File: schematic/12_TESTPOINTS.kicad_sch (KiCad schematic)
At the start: 10 parts

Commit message: Exclude JP1, JP2, TP1-TP20 from BOM (attrs only, sch+pcb)
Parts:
- TP11, TP12, TP13, TP14, TP15, TP16, TP17, TP18, TP19, TP20: now left out of the parts list
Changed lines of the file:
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@@
 		(unit 1)
 		(exclude_from_sim no)
-		(in_bom yes)
+		(in_bom no)
 		(on_board yes)
 		(dnp no)
@@
 		(unit 1)
 		(exclude_from_sim no)
-		(in_bom yes)
+		(in_bom no)
 		(on_board yes)
 		(dnp no)
@@
 		(unit 1)
 		(exclude_from_sim no)
-		(in_bom yes)
+		(in_bom no)
 		(on_board yes)
 		(dnp no)
@@
 		(unit 1)
 		(exclude_from_sim no)
-		(in_bom yes)
+		(in_bom no)
 		(on_board yes)
 		(dnp no)
@@
 		(unit 1)
 		(exclude_from_sim no)
-		(in_bom yes)
+		(in_bom no)
 		(on_board yes)
 		(dnp no)
@@
 		(unit 1)
 		(exclude_from_sim no)
-		(in_bom yes)
+		(in_bom no)
 		(on_board yes)
 		(dnp no)
@@
 		(unit 1)
 		(exclude_from_sim no)
-		(in_bom yes)
+		(in_bom no)
 		(on_board yes)
 		(dnp no)
@@
 		(unit 1)
 		(exclude_from_sim no)
-		(in_bom yes)
+		(in_bom no)
 		(on_board yes)
 		(dnp no)
@@
 		(unit 1)
 		(exclude_from_sim no)
-		(in_bom yes)
+		(in_bom no)
 		(on_board yes)
 		(dnp no)
@@
 		(unit 1)
 		(exclude_from_sim no)
-		(in_bom yes)
-		(on_board yes)
-		(dnp no)
+		(in_bom no)
+		(on_board yes)
+		(dnp no)

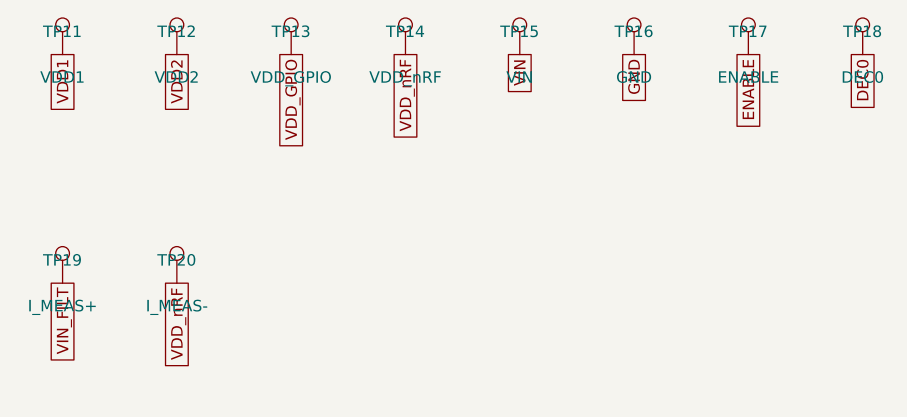
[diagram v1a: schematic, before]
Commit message: v2: simplify to UART modem module (J20 host header, LXC translators); remove J1, J3, J6, J9-J18, optional parts
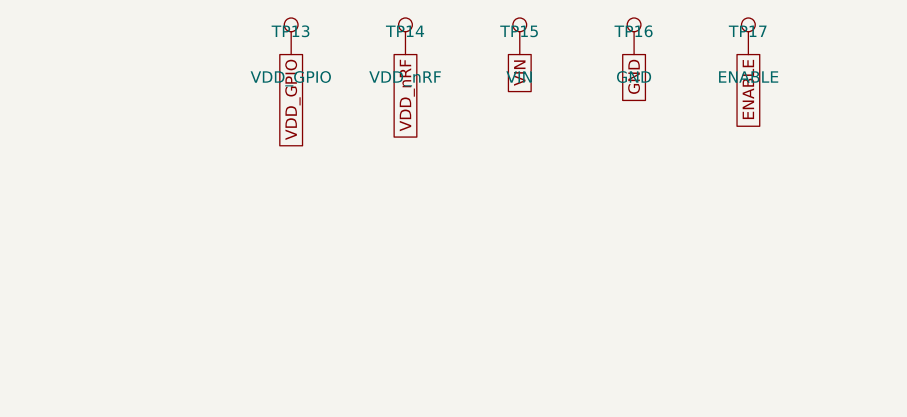
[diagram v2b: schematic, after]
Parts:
- removed TP11: VDD1, TestPoint:TestPoint_Pad_D1.5mm, symbol Connector:TestPoint
- removed TP12: VDD2, TestPoint:TestPoint_Pad_D1.5mm, symbol Connector:TestPoint
- removed TP18: DEC0, TestPoint:TestPoint_Pad_D1.5mm, symbol Connector:TestPoint
- removed TP19: I_MEAS+, TestPoint:TestPoint_Pad_D1.5mm, symbol Connector:TestPoint
- removed TP20: I_MEAS-, TestPoint:TestPoint_Pad_D1.5mm, symbol Connector:TestPoint
